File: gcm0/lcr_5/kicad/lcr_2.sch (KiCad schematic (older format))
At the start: 146 parts, among them J1 5V, J2 -5V, J3 Conn_01x01_Male, J7 sin, Q1 BC547, Q2 BC547, Q3 BC547, SW1 1, SW2 2, SW3 SW_DIP_x01, U1 MC4580G-S08-R, U10 MC4580G-S08-R, U11 74HC595, U12 STM32F030F4P6, U13 L7809, U2 74HC4053PW,112, U3 74HC4052PW,118, U4 MC4580G-S08-R, U5 LM2596S-5, U6 LM7805_TO220, U7 MC4580G-S08-R, U8 LM1117-3.3, U9 74HC4053PW,112, Y1 8M

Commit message: 修改模拟电路
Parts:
- removed C49, C50: 470uF, symbol Device:CP
- removed R33: 100, symbol Device:R
- removed R34, R36: 1K, symbol Device:R
- added J4: SWD, Connector_PinHeader_2.54mm:PinHeader_1x03_P2.54mm_Vertical, symbol Connector:Conn_01x03_Male
- added L? (x2): 47uH, Inductor_THT:L_Radial_D6.0mm_P4.00mm, symbol Device:L_Core_Ferrite
- C1, C11, C24, C25, C26, C29, C30, C32, C33, C34, C37, C38, C6, C7: value 104 -> 106; footprint Capacitor_SMD:C_0603_1608Metric_Pad1.08x0.95mm_HandSolder -> Capacitor_SMD:C_0805_2012Metric_Pad1.18x1.45mm_HandSolder
- C10, C12, C13, C15, C16, C17, C18, C19, C2, C36, C4, C40, C41, C42, C43, C44, C5, C8, C9: footprint Capacitor_SMD:C_0603_1608Metric_Pad1.08x0.95mm_HandSolder -> Capacitor_SMD:C_0805_2012Metric_Pad1.18x1.45mm_HandSolder
- C47: value 15 -> 22; footprint Capacitor_SMD:C_0603_1608Metric_Pad1.08x0.95mm_HandSolder -> Capacitor_SMD:C_0805_2012Metric_Pad1.18x1.45mm_HandSolder
- C48: footprint (none) -> Capacitor_SMD:C_0805_2012Metric_Pad1.18x1.45mm_HandSolder
- D11, D12, D13, D14: footprint Diode_THT:D_DO-41_SOD81_P10.16mm_Horizontal -> Diode_THT:D_DO-41_SOD81_P2.54mm_Vertical_AnodeUp
- R1, R10, R12, R13, R14, R15, R16, R17, R18, R19, R2, R20, R21, R22, R25, R26, R27, R28, R3, R30, R32, R35, R37, R4, R42, R43, R44, R45, R46, R47, R48, R49, R50, R51, R52, R7, R8, R9: footprint Resistor_THT:R_Axial_DIN0204_L3.6mm_D1.6mm_P1.90mm_Vertical -> Resistor_SMD:R_0805_2012Metric_Pad1.20x1.40mm_HandSolder
- R11: value 100 -> 1K; footprint Resistor_THT:R_Axial_DIN0204_L3.6mm_D1.6mm_P1.90mm_Vertical -> Resistor_SMD:R_0805_2012Metric_Pad1.20x1.40mm_HandSolder
- R23, R24: value 1K -> 100; footprint Resistor_THT:R_Axial_DIN0204_L3.6mm_D1.6mm_P1.90mm_Vertical -> Resistor_SMD:R_0805_2012Metric_Pad1.20x1.40mm_HandSolder
- R29, R31, R5, R6: value 20K -> 10K; footprint (none) -> Resistor_SMD:R_0805_2012Metric_Pad1.20x1.40mm_HandSolder
- R38, R39, R40, R41, R53, R54, R55, R56, R57: footprint (none) -> Resistor_SMD:R_0805_2012Metric_Pad1.20x1.40mm_HandSolder
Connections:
- net +5V: now also L?.1; no longer C1.1, C11.2, C25.1, C29.1, C32.2, C33.1, C37.1, U1.8 (V+), U10.8 (V+), U2.16 (VDD), U3.16 (VDD), U4.8 (V+), U7.8 (V+), U9.16 (VDD)
- net -5V: now also L?.2; no longer C24.1, C26.1, C30.1, C34.1, C38.1, C6.1, C7.2, U1.4 (V-), U10.4 (V-), U2.7 (VEE), U3.7 (VEE), U4.4 (V-), U7.4 (V-), U9.7 (VEE)
- net CLK: now also J4.2 (Pin_2)
- net DIO: now also J4.3 (Pin_3)
- net GND: now also J4.1 (Pin_1)
- net at R23.2, U4.1: now also U4.2 (-)
- net at U4.6 (-): now also R24.2, U4.7
- new net +5VA: C1.1, C11.2, C25.1, C29.1, C32.2, C33.1, C37.1, L?.2, U1.8 (V+), U10.8 (V+), U2.16 (VDD), U3.16 (VDD), U4.8 (V+), U7.8 (V+), U9.16 (VDD)
- new net -5VA: C24.1, C26.1, C30.1, C34.1, C38.1, C6.1, C7.2, L?.1, U1.4 (V-), U10.4 (V-), U2.7 (VEE), U3.7 (VEE), U4.4 (V-), U7.4 (V-), U9.7 (VEE)
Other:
- moved on the sheet: U4A, U4B

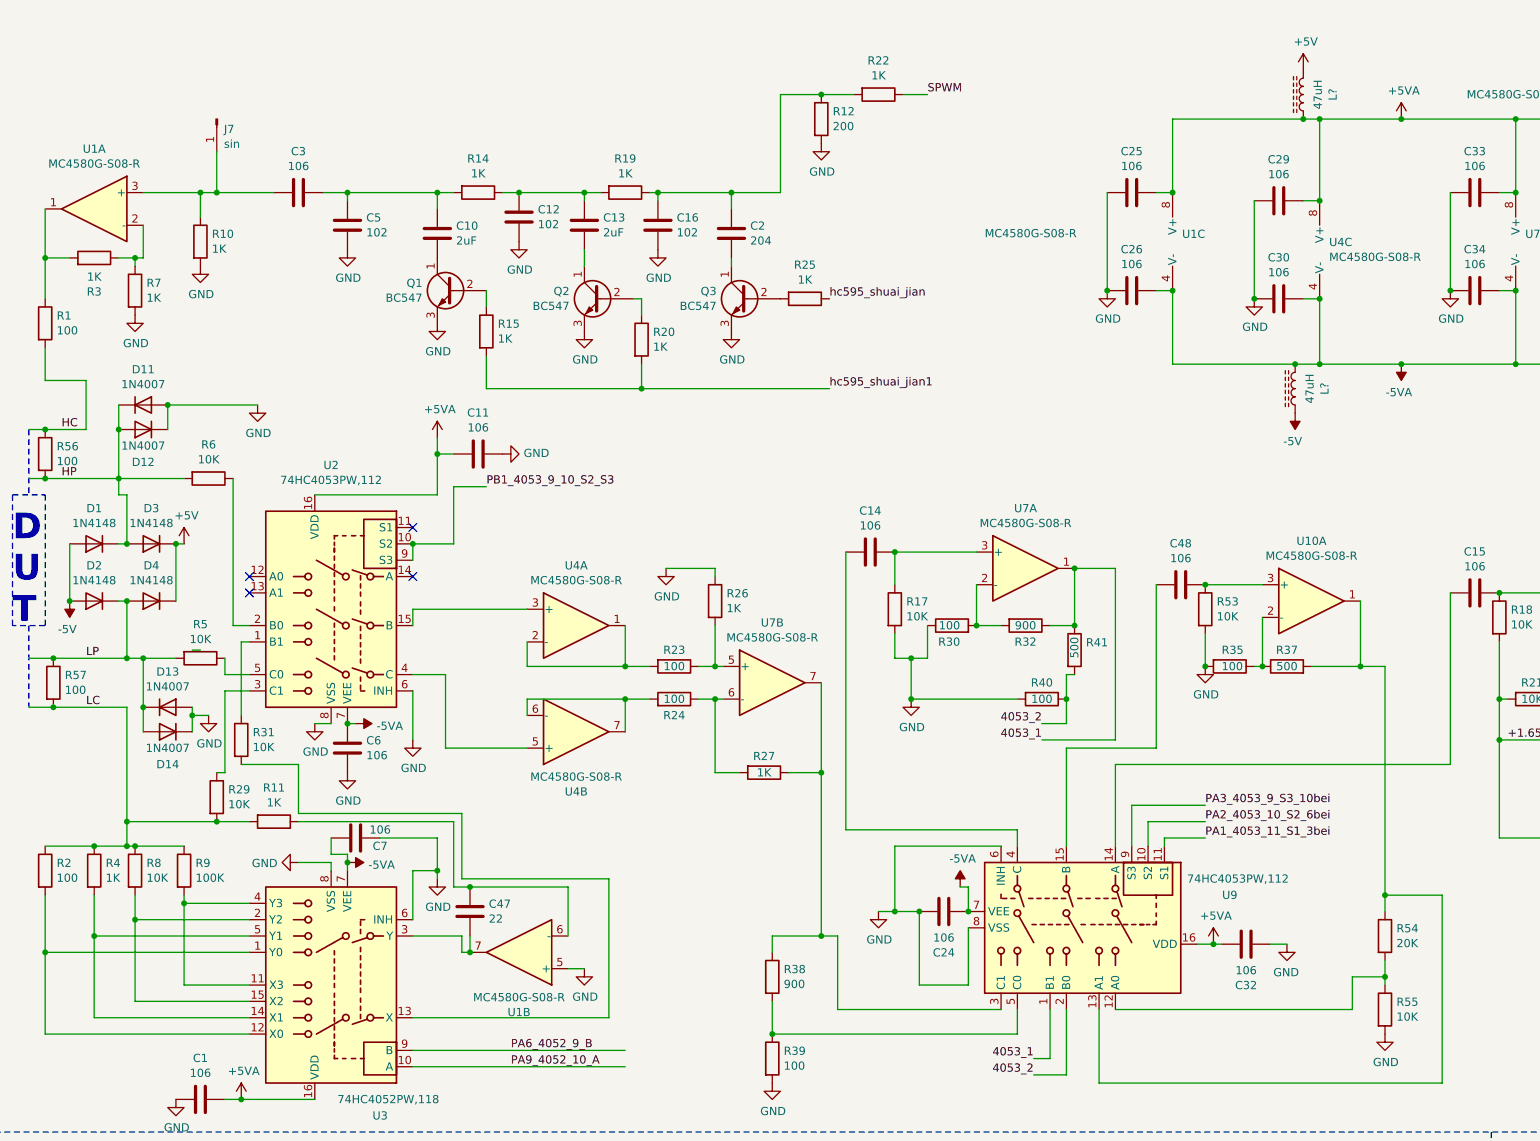
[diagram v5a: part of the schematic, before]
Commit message: 修改三倍衰减电阻
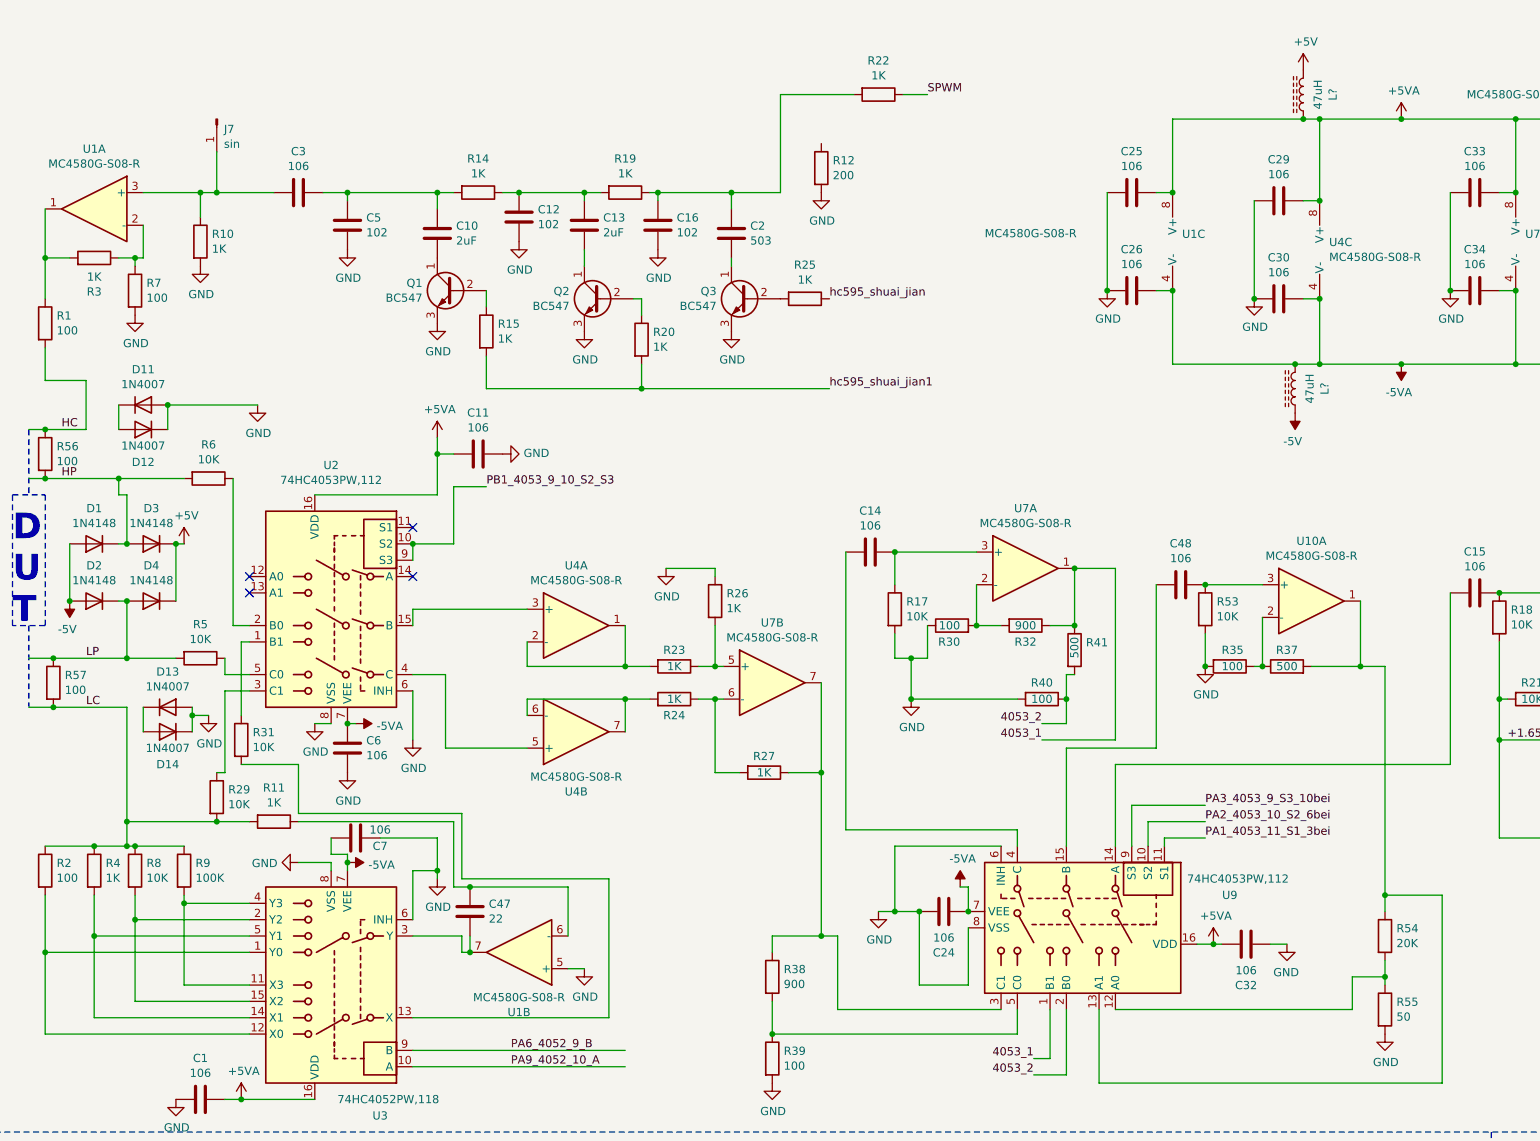
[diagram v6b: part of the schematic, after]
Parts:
- C2: value 204 -> 503
- R23, R24: value 100 -> 1K
- R55: value 10K -> 50
- R7: value 1K -> 100
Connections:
- net HP: no longer D11.1 (K), D12.2 (A)
- net LP: no longer D13.1 (K), D14.2 (A)
- net at C16.1, C2.1, R19.1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: no longer R12.1
- new net: D11.1 (K), D12.2 (A)
- new net: D13.1 (K), D14.2 (A)
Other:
- moved on the sheet: R12
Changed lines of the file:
@@
 P 4650 4450
 F 0 "R23" V 4550 4450 50  0000 C CNN
-F 1 "100" V 4650 4450 50  0000 C CNN
+F 1 "1K" V 4650 4450 50  0000 C CNN
 F 2 "Resistor_SMD:R_0805_2012Metric_Pad1.20x1.40mm_HandSolder" V 4580 4450 50  0001 C CNN
 F 3 "~" H 4650 4450 50  0001 C CNN
@@
 P 4650 4650
 F 0 "R24" V 4550 4650 50  0000 C CNN
-F 1 "100" V 4650 4650 50  0000 C CNN
+F 1 "1K" V 4650 4650 50  0000 C CNN
 F 2 "Resistor_SMD:R_0805_2012Metric_Pad1.20x1.40mm_HandSolder" V 4580 4650 50  0001 C CNN
 F 3 "~" H 4650 4650 50  0001 C CNN
@@
 	800  1950 800  1650
 $Comp
-L Device:R R7
-U 1 1 61F0532D
-P 1350 2150
-F 0 "R7" H 1420 2196 50  0000 L CNN
-F 1 "1K" H 1420 2105 50  0000 L CNN
-F 2 "Resistor_SMD:R_0805_2012Metric_Pad1.20x1.40mm_HandSolder" V 1280 2150 50  0001 C CNN
-F 3 "~" H 1350 2150 50  0001 C CNN
-	1    1350 2150
-	1    0    0    -1
-$EndComp
-$Comp
 L power:GND #PWR03
 U 1 1 61F072FE
@@
 P 5000 1800
 F 0 "C2" H 5115 1846 50  0000 L CNN
-F 1 "204" H 5115 1755 50  0000 L CNN
+F 1 "503" H 5115 1755 50  0000 L CNN
 F 2 "Capacitor_SMD:C_0805_2012Metric_Pad1.18x1.45mm_HandSolder" H 5038 1650 50  0001 C CNN
 F 3 "~" H 5000 1800 50  0001 C CNN
@@
 Connection ~ 3400 6200
 Wire Wire Line
-	5750 950  5550 950
-Wire Wire Line
 	5300 950  5300 1550
 $Comp
 L Device:R R12
 U 1 1 621239DC
-P 5550 1100
-F 0 "R12" H 5620 1146 50  0000 L CNN
-F 1 "200" H 5620 1055 50  0000 L CNN
-F 2 "Resistor_SMD:R_0805_2012Metric_Pad1.20x1.40mm_HandSolder" V 5480 1100 50  0001 C CNN
-F 3 "~" H 5550 1100 50  0001 C CNN
-	1    5550 1100
+P 5550 1400
+F 0 "R12" H 5620 1446 50  0000 L CNN
+F 1 "200" H 5620 1355 50  0000 L CNN
+F 2 "Resistor_SMD:R_0805_2012Metric_Pad1.20x1.40mm_HandSolder" V 5480 1400 50  0001 C CNN
+F 3 "~" H 5550 1400 50  0001 C CNN
+	1    5550 1400
 	1    0    0    -1
 $EndComp
-Connection ~ 5550 950
-Wire Wire Line
-	5550 950  5300 950
 $Comp
 L power:GND #PWR09
 U 1 1 621257B8
-P 5550 1250
-F 0 "#PWR09" H 5550 1000 50  0001 C CNN
-F 1 "GND" H 5555 1077 50  0000 C CNN
-F 2 "" H 5550 1250 50  0001 C CNN
-F 3 "" H 5550 1250 50  0001 C CNN
-	1    5550 1250
+P 5550 1550
+F 0 "#PWR09" H 5550 1300 50  0001 C CNN
+F 1 "GND" H 5555 1377 50  0000 C CNN
+F 2 "" H 5550 1550 50  0001 C CNN
+F 3 "" H 5550 1550 50  0001 C CNN
+	1    5550 1550
 	1    0    0    -1
 $EndComp
@@
 Connection ~ 9700 4000
 $Comp
-L Device:R R54
-U 1 1 641F07B2
-P 9000 6100
-F 0 "R54" H 9070 6146 50  0000 L CNN
-F 1 "20K" H 9070 6055 50  0000 L CNN
-F 2 "Resistor_SMD:R_0805_2012Metric_Pad1.20x1.40mm_HandSolder" V 8930 6100 50  0001 C CNN
-F 3 "~" H 9000 6100 50  0001 C CNN
-	1    9000 6100
-	1    0    0    -1
-$EndComp
-$Comp
 L Device:R R55
 U 1 1 641F24CF
 P 9000 6550
 F 0 "R55" H 9070 6596 50  0000 L CNN
-F 1 "10K" H 9070 6505 50  0000 L CNN
+F 1 "50" H 9070 6505 50  0000 L CNN
 F 2 "Resistor_SMD:R_0805_2012Metric_Pad1.20x1.40mm_HandSolder" V 8930 6550 50  0001 C CNN
 F 3 "~" H 9000 6550 50  0001 C CNN
@@
 	3300 3350 3500 3350
 Wire Wire Line
-	1750 4350 1700 4350
-Wire Wire Line
 	5550 5100 5550 6100
 $Comp
@@
 Wire Wire Line
 	7700 1550 7700 1100
-Wire Wire Line
-	1700 4750 1700 4850
-Wire Wire Line
-	1800 4750 1700 4750
-Connection ~ 1700 4750
-Wire Wire Line
-	1700 4700 1700 4750
-$Comp
-L power:GND #PWR039
-U 1 1 629AA0F3
-P 1800 4750
-F 0 "#PWR039" H 1800 4500 50  0001 C CNN
-F 1 "GND" H 1805 4577 50  0000 C CNN
-F 2 "" H 1800 4750 50  0001 C CNN
-F 3 "" H 1800 4750 50  0001 C CNN
-	1    1800 4750
-	1    0    0    -1
-$EndComp
-Wire Wire Line
-	1550 2850 2100 2850
-Wire Wire Line
-	1550 3000 1550 2850
-$Comp
-L power:GND #PWR042
-U 1 1 62578CEA
-P 2100 2850
-F 0 "#PWR042" H 2100 2600 50  0001 C CNN
-F 1 "GND" H 2105 2677 50  0000 C CNN
-F 2 "" H 2100 2850 50  0001 C CNN
-F 3 "" H 2100 2850 50  0001 C CNN
-	1    2100 2850
-	1    0    0    -1
-$EndComp
-Wire Wire Line
-	1600 4400 1400 4400
-Connection ~ 1400 4400
-Connection ~ 1400 4700
-Wire Wire Line
-	1400 4700 1400 4400
-Wire Wire Line
-	1400 4850 1400 4700
-$Comp
-L Diode:1N4007 D14
-U 1 1 626C93AB
-P 1550 4850
-F 0 "D14" H 1550 5050 50  0000 C CNN
-F 1 "1N4007" H 1550 4950 50  0000 C CNN
-F 2 "Diode_THT:D_DO-41_SOD81_P2.54mm_Vertical_AnodeUp" H 1550 4675 50  0001 C CNN
-F 3 "http://www.vishay.com/docs/88503/1n4001.pdf" H 1550 4850 50  0001 C CNN
-	1    1550 4850
-	-1   0    0    1
-$EndComp
-$Comp
-L Diode:1N4007 D13
-U 1 1 626C7C25
-P 1550 4700
-F 0 "D13" H 1550 4917 50  0000 C CNN
-F 1 "1N4007" H 1550 4826 50  0000 C CNN
-F 2 "Diode_THT:D_DO-41_SOD81_P2.54mm_Vertical_AnodeUp" H 1550 4525 50  0001 C CNN
-F 3 "http://www.vishay.com/docs/88503/1n4001.pdf" H 1550 4700 50  0001 C CNN
-	1    1550 4700
-	1    0    0    -1
-$EndComp
 Connection ~ 1250 3300
-Connection ~ 1550 2850
-Connection ~ 1250 3000
-Wire Wire Line
-	1250 3000 1250 3300
-Wire Wire Line
-	1250 2850 1250 3000
 Wire Wire Line
 	1650 3300 1250 3300
 Wire Wire Line
 	800  3300 1250 3300
-$Comp
-L Diode:1N4007 D12
-U 1 1 624EBBB9
-P 1400 3000
-F 0 "D12" H 1400 3200 50  0000 C CNN
-F 1 "1N4007" H 1400 3100 50  0000 C CNN
-F 2 "Diode_THT:D_DO-41_SOD81_P2.54mm_Vertical_AnodeUp" H 1400 2825 50  0001 C CNN
-F 3 "http://www.vishay.com/docs/88503/1n4001.pdf" H 1400 3000 50  0001 C CNN
-	1    1400 3000
-	-1   0    0    1
-$EndComp
-$Comp
-L Diode:1N4007 D11
-U 1 1 624E92F8
-P 1400 2850
-F 0 "D11" H 1400 3067 50  0000 C CNN
-F 1 "1N4007" H 1400 2976 50  0000 C CNN
-F 2 "Diode_THT:D_DO-41_SOD81_P2.54mm_Vertical_AnodeUp" H 1400 2675 50  0001 C CNN
-F 3 "http://www.vishay.com/docs/88503/1n4001.pdf" H 1400 2850 50  0001 C CNN
-	1    1400 2850
-	1    0    0    -1
-$EndComp
 Wire Wire Line
 	1650 3700 1600 3700
@@
 Wire Wire Line
 	850  4400 1300 4400
-Wire Wire Line
-	1400 4400 1300 4400
 Connection ~ 1300 4400
 Wire Wire Line
@@
 Wire Wire Line
 	4350 4650 4500 4650
+Wire Wire Line
+	5300 950  5750 950
+$Comp
+L Device:R R7
+U 1 1 61F0532D
+P 1350 2150
+F 0 "R7" H 1420 2196 50  0000 L CNN
+F 1 "100" H 1420 2105 50  0000 L CNN
+F 2 "Resistor_SMD:R_0805_2012Metric_Pad1.20x1.40mm_HandSolder" V 1280 2150 50  0001 C CNN
+F 3 "~" H 1350 2150 50  0001 C CNN
+	1    1350 2150
+	1    0    0    -1
+$EndComp
+$Comp
+L Diode:1N4007 D13
+U 1 1 626C7C25
+P 1550 4700
+F 0 "D13" H 1550 4917 50  0000 C CNN
+F 1 "1N4007" H 1550 4826 50  0000 C CNN
+F 2 "Diode_THT:D_DO-41_SOD81_P2.54mm_Vertical_AnodeUp" H 1550 4525 50  0001 C CNN
+F 3 "http://www.vishay.com/docs/88503/1n4001.pdf" H 1550 4700 50  0001 C CNN
+	1    1550 4700
+	1    0    0    -1
+$EndComp
+$Comp
+L Diode:1N4007 D14
+U 1 1 626C93AB
+P 1550 4850
+F 0 "D14" H 1550 5050 50  0000 C CNN
+F 1 "1N4007" H 1550 4950 50  0000 C CNN
+F 2 "Diode_THT:D_DO-41_SOD81_P2.54mm_Vertical_AnodeUp" H 1550 4675 50  0001 C CNN
+F 3 "http://www.vishay.com/docs/88503/1n4001.pdf" H 1550 4850 50  0001 C CNN
+	1    1550 4850
+	-1   0    0    1
+$EndComp
+Wire Wire Line
+	1400 4850 1400 4700
+$Comp
+L power:GND #PWR039
+U 1 1 629AA0F3
+P 1800 4750
+F 0 "#PWR039" H 1800 4500 50  0001 C CNN
+F 1 "GND" H 1805 4577 50  0000 C CNN
+F 2 "" H 1800 4750 50  0001 C CNN
+F 3 "" H 1800 4750 50  0001 C CNN
+	1    1800 4750
+	1    0    0    -1
+$EndComp
+Wire Wire Line
+	1700 4700 1700 4750
+Wire Wire Line
+	1800 4750 1700 4750
+Connection ~ 1700 4750
+Wire Wire Line
+	1700 4750 1700 4850
+$Comp
+L power:GND #PWR042
+U 1 1 62578CEA
+P 2100 2850
+F 0 "#PWR042" H 2100 2600 50  0001 C CNN
+F 1 "GND" H 2105 2677 50  0000 C CNN
+F 2 "" H 2100 2850 50  0001 C CNN
+F 3 "" H 2100 2850 50  0001 C CNN
+	1    2100 2850
+	1    0    0    -1
+$EndComp
+$Comp
+L Diode:1N4007 D11
+U 1 1 624E92F8
+P 1400 2850
+F 0 "D11" H 1400 3067 50  0000 C CNN
+F 1 "1N4007" H 1400 2976 50  0000 C CNN
+F 2 "Diode_THT:D_DO-41_SOD81_P2.54mm_Vertical_AnodeUp" H 1400 2675 50  0001 C CNN
+F 3 "http://www.vishay.com/docs/88503/1n4001.pdf" H 1400 2850 50  0001 C CNN
+	1    1400 2850
+	1    0    0    -1
+$EndComp
+$Comp
+L Diode:1N4007 D12
+U 1 1 624EBBB9
+P 1400 3000
+F 0 "D12" H 1400 3200 50  0000 C CNN
+F 1 "1N4007" H 1400 3100 50  0000 C CNN
+F 2 "Diode_THT:D_DO-41_SOD81_P2.54mm_Vertical_AnodeUp" H 1400 2825 50  0001 C CNN
+F 3 "http://www.vishay.com/docs/88503/1n4001.pdf" H 1400 3000 50  0001 C CNN
+	1    1400 3000
+	-1   0    0    1
+$EndComp
+Wire Wire Line
+	1250 2850 1250 3000
+Wire Wire Line
+	1550 3000 1550 2850
+Connection ~ 1550 2850
+Wire Wire Line
+	1550 2850 2100 2850
+$Comp
+L Device:R R54
+U 1 1 641F07B2
+P 9000 6100
+F 0 "R54" H 9070 6146 50  0000 L CNN
+F 1 "20K" H 9070 6055 50  0000 L CNN
+F 2 "Resistor_SMD:R_0805_2012Metric_Pad1.20x1.40mm_HandSolder" V 8930 6100 50  0001 C CNN
+F 3 "~" H 9000 6100 50  0001 C CNN
+	1    9000 6100
+	1    0    0    -1
+$EndComp
+Wire Wire Line
+	1300 4400 1600 4400
 $EndSCHEMATC
